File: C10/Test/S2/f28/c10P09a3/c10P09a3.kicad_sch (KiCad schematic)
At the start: 5 parts

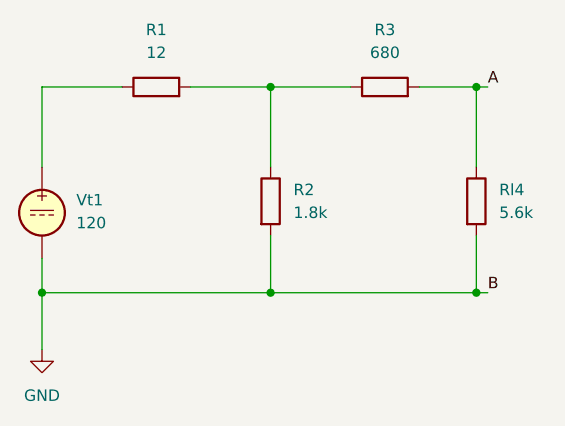
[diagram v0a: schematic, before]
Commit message: corrected from misprinting Fig 10-28
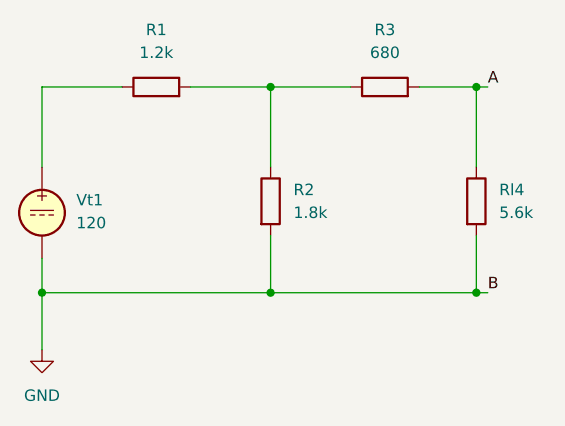
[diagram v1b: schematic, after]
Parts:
- R1: value 12 -> 1.2k
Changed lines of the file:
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@@
 			)
 		)
-		(property "Value" "12"
+		(property "Value" "1.2k"
 			(at 148.59 67.31 90)
 			(show_name no)
